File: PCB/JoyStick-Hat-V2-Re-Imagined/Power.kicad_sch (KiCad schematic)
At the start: 14 parts, among them J6 1757242, M2 D24V22F5, M3 D24V22F3

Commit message: Joystick Hat V2 Progress
Powersupply section laid out on V2 of JoyStick Hat PCB
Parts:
- C21: footprint AVR-KiCAD-Lib-Capacitors:CP_Elec_4x5.3 -> AVR-KiCAD-Lib-Capacitors:CAP_UUQ_6P3X5P4_NCH
- C22: footprint AVR-KiCAD-Lib-Capacitors:CP_Elec_4x5.3 -> AVR-KiCAD-Lib-Capacitors:CAP_UUQ_4X5P4_NCH
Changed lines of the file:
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@@
 			)
 		)
-		(property "Footprint" "AVR-KiCAD-Lib-Capacitors:CP_Elec_4x5.3"
+		(property "Footprint" "AVR-KiCAD-Lib-Capacitors:CAP_UUQ_4X5P4_NCH"
 			(at 124.46 127 0)
 			(effects
@@
 			)
 		)
-		(property "Footprint" "AVR-KiCAD-Lib-Capacitors:CP_Elec_4x5.3"
+		(property "Footprint" "AVR-KiCAD-Lib-Capacitors:CAP_UUQ_6P3X5P4_NCH"
 			(at 111.76 127 0)
 			(effects

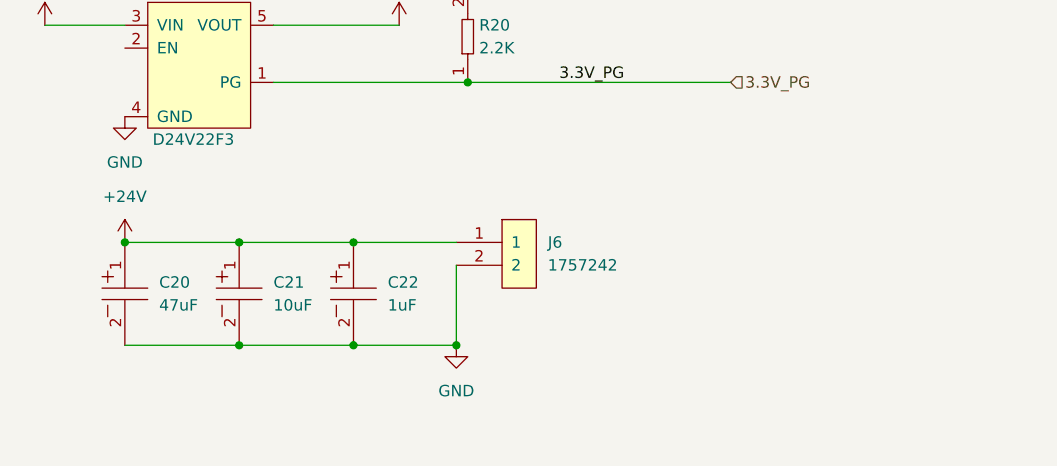
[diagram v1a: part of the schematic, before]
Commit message: V2 Tweaks
More Tweaks to the completed V2 design. 3D renders of V2 design produced and added to img folder for documentation update coming in the next commit. Photos of prototype also added to img folder for documentation.
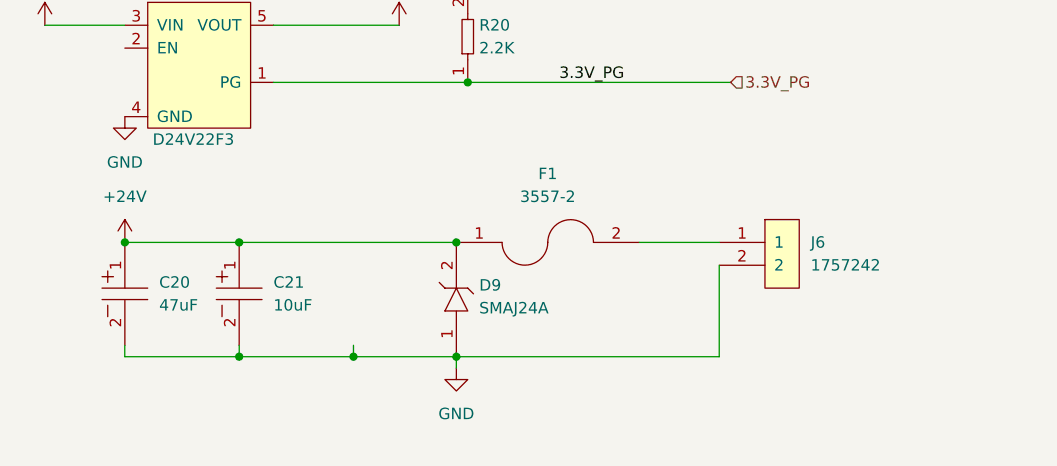
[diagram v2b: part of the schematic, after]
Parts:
- removed C22: UUQ1H010MCL1GB, AVR-KiCAD-Lib-Capacitors:CAP_UUQ_4X5P4_NCH, symbol AVR-KiCAD-Lib-Capacitors:UUQ1H010MCL1GB
- added D9: SMAJ24A, AVR-KiCAD-Lib-Diodes:SMAJ, symbol AVR-KiCAD-Lib-Diodes:SMAJ24A
- added F1: 3557-2, AVR-KiCAD-Lib-Fuse-Holders:FUSE_3557-2, symbol AVR-KiCAD-Lib-Fuse-Holders:3557-2
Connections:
- net +24V: now also D9.2, F1.1; no longer J6.1
- net GND: now also D9.1
- new net: F1.2, J6.1
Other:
- moved on the sheet: J6

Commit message: STM32 Exp
Removed 5V regulator, corrected RS485 schematic,  added more expansion to STM32 since we had space.
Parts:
- removed M2: D24V22F5, AVR-KiCAD-Lib-Modules:D24V22F12, symbol AVR-KiCAD-Lib-Modules:D24V22F5
- removed R21: RC0603FR-072K2L, AVR-KiCAD-Lib-Resistors:R0603, symbol AVR-KiCAD-Lib-Resistors:RC0603FR-072K2L
